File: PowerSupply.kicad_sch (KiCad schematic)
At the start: 3 parts

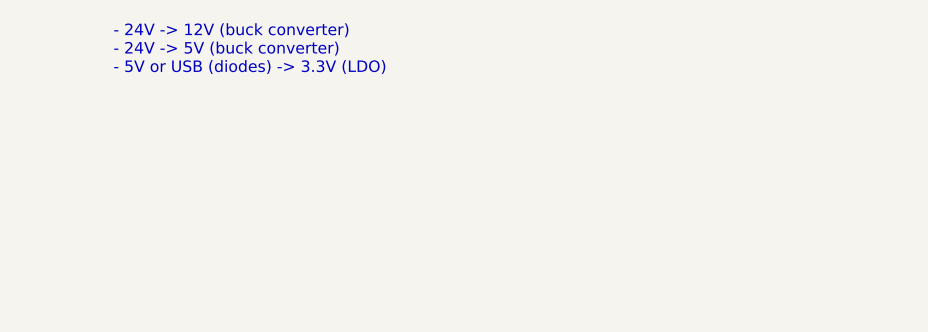
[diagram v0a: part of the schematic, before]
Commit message: Assigning a lot of values to components Change MOSFETS for different (correct) ones Copy Motor1 to Motor2-4 Guess max current per voltage on PowerSupply schema
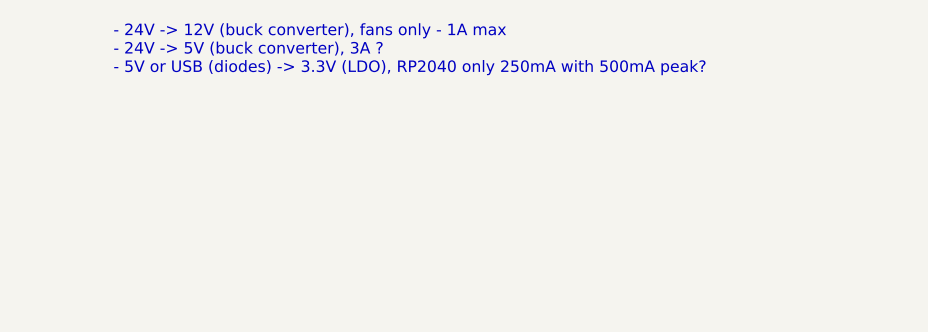
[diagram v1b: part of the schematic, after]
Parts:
- J?: footprint (none) -> Connector_USB:USB_C_Receptacle_GCT_USB4105-xx-A_16P_TopMnt_Horizontal; LCSC (none) -> C2765186
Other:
- note added: "- 24V -> 12V (buck converter), fans only - 1A max - 24V -> 5V (buck converter), 3A ? - 5V or USB (diodes) -> 3.3V (LDO), RP2040 only 250mA with 500mA peak?"
- note removed: "- 24V -> 12V (buck converter) - 24V -> 5V (buck converter) - 5V or USB (diodes) -> 3.3V (LDO)"
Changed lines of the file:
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@@
     (stroke (width 0) (type default))
   )
-  (text "- 24V -> 12V (buck converter)\n- 24V -> 5V (buck converter)\n- 5V or USB (diodes) -> 3.3V (LDO)"
+  (text "- 24V -> 12V (buck converter), fans only - 1A max\n- 24V -> 5V (buck converter), 3A ?\n- 5V or USB (diodes) -> 3.3V (LDO), RP2040 only 250mA with 500mA peak?"
     (at 30.48 34.29 0)
     (effects (font (size 1.27 1.27)) (justify left bottom))
@@
       )
       (project "Can3DPrinter4Motor"
-        (path "/cb4e159a-5c17-494a-ba7f-10e700f814f1/48301791-0cbb-476d-b990-e4256493ff46"
-          (reference "#PWR?") (unit 1)
-        )
         (path "/cb4e159a-5c17-494a-ba7f-10e700f814f1/03ab3e80-f454-40c8-8f97-43a0b791de0b"
           (reference "#PWR0402") (unit 1)
+        )
+        (path "/cb4e159a-5c17-494a-ba7f-10e700f814f1/48301791-0cbb-476d-b990-e4256493ff46"
+          (reference "#PWR0302") (unit 1)
         )
       )
@@
       (effects (font (size 1.27 1.27)))
     )
-    (property "Footprint" "" (at 38.1 165.1 0)
-      (effects (font (size 1.27 1.27)) hide)
-    )
-    (property "Datasheet" "https://www.usb.org/sites/default/files/documents/usb_type-c.zip" (at 38.1 165.1 0)
-      (effects (font (size 1.27 1.27)) hide)
-    )
-    (property "LCSC" "" (at 34.29 165.1 0)
+    (property "Footprint" "Connector_USB:USB_C_Receptacle_GCT_USB4105-xx-A_16P_TopMnt_Horizontal" (at 38.1 165.1 0)
+      (effects (font (size 1.27 1.27)) hide)
+    )
+    (property "Datasheet" "https://datasheet.lcsc.com/lcsc/2111231930_SHOU-HAN-TYPE-C-16PIN-2MD-073_C2765186.pdf" (at 38.1 165.1 0)
+      (effects (font (size 1.27 1.27)) hide)
+    )
+    (property "LCSC" "C2765186" (at 34.29 165.1 0)
       (effects (font (size 1.27 1.27)) hide)
     )
@@
     (instances
       (project "Can3DPrinter4Motor"
-        (path "/cb4e159a-5c17-494a-ba7f-10e700f814f1/48301791-0cbb-476d-b990-e4256493ff46"
+        (path "/cb4e159a-5c17-494a-ba7f-10e700f814f1/03ab3e80-f454-40c8-8f97-43a0b791de0b"
           (reference "J?") (unit 1)
         )
-        (path "/cb4e159a-5c17-494a-ba7f-10e700f814f1/03ab3e80-f454-40c8-8f97-43a0b791de0b"
-          (reference "J?") (unit 1)
+        (path "/cb4e159a-5c17-494a-ba7f-10e700f814f1/48301791-0cbb-476d-b990-e4256493ff46"
+          (reference "J301") (unit 1)
         )
       )
@@
           (reference "R?") (unit 1)
         )
-        (path "/cb4e159a-5c17-494a-ba7f-10e700f814f1/48301791-0cbb-476d-b990-e4256493ff46"
-          (reference "R?") (unit 1)
-        )
-        (path "/cb4e159a-5c17-494a-ba7f-10e700f814f1/03ab3e80-f454-40c8-8f97-43a0b791de0b"
-          (reference "R?") (unit 1)
+        (path "/cb4e159a-5c17-494a-ba7f-10e700f814f1/03ab3e80-f454-40c8-8f97-43a0b791de0b"
+          (reference "R?") (unit 1)
+        )
+        (path "/cb4e159a-5c17-494a-ba7f-10e700f814f1/48301791-0cbb-476d-b990-e4256493ff46"
+          (reference "R302") (unit 1)
         )
       )
@@
           (reference "R?") (unit 1)
         )
-        (path "/cb4e159a-5c17-494a-ba7f-10e700f814f1/48301791-0cbb-476d-b990-e4256493ff46"
-          (reference "R?") (unit 1)
-        )
-        (path "/cb4e159a-5c17-494a-ba7f-10e700f814f1/03ab3e80-f454-40c8-8f97-43a0b791de0b"
-          (reference "R?") (unit 1)
+        (path "/cb4e159a-5c17-494a-ba7f-10e700f814f1/03ab3e80-f454-40c8-8f97-43a0b791de0b"
+          (reference "R?") (unit 1)
+        )
+        (path "/cb4e159a-5c17-494a-ba7f-10e700f814f1/48301791-0cbb-476d-b990-e4256493ff46"
+          (reference "R301") (unit 1)
         )
       )
@@
       )
       (project "Can3DPrinter4Motor"
-        (path "/cb4e159a-5c17-494a-ba7f-10e700f814f1/48301791-0cbb-476d-b990-e4256493ff46"
-          (reference "#PWR?") (unit 1)
-        )
         (path "/cb4e159a-5c17-494a-ba7f-10e700f814f1/03ab3e80-f454-40c8-8f97-43a0b791de0b"
           (reference "#PWR0401") (unit 1)
         )
-      )
+        (path "/cb4e159a-5c17-494a-ba7f-10e700f814f1/48301791-0cbb-476d-b990-e4256493ff46"
+          (reference "#PWR0301") (unit 1)
+        )
+      )

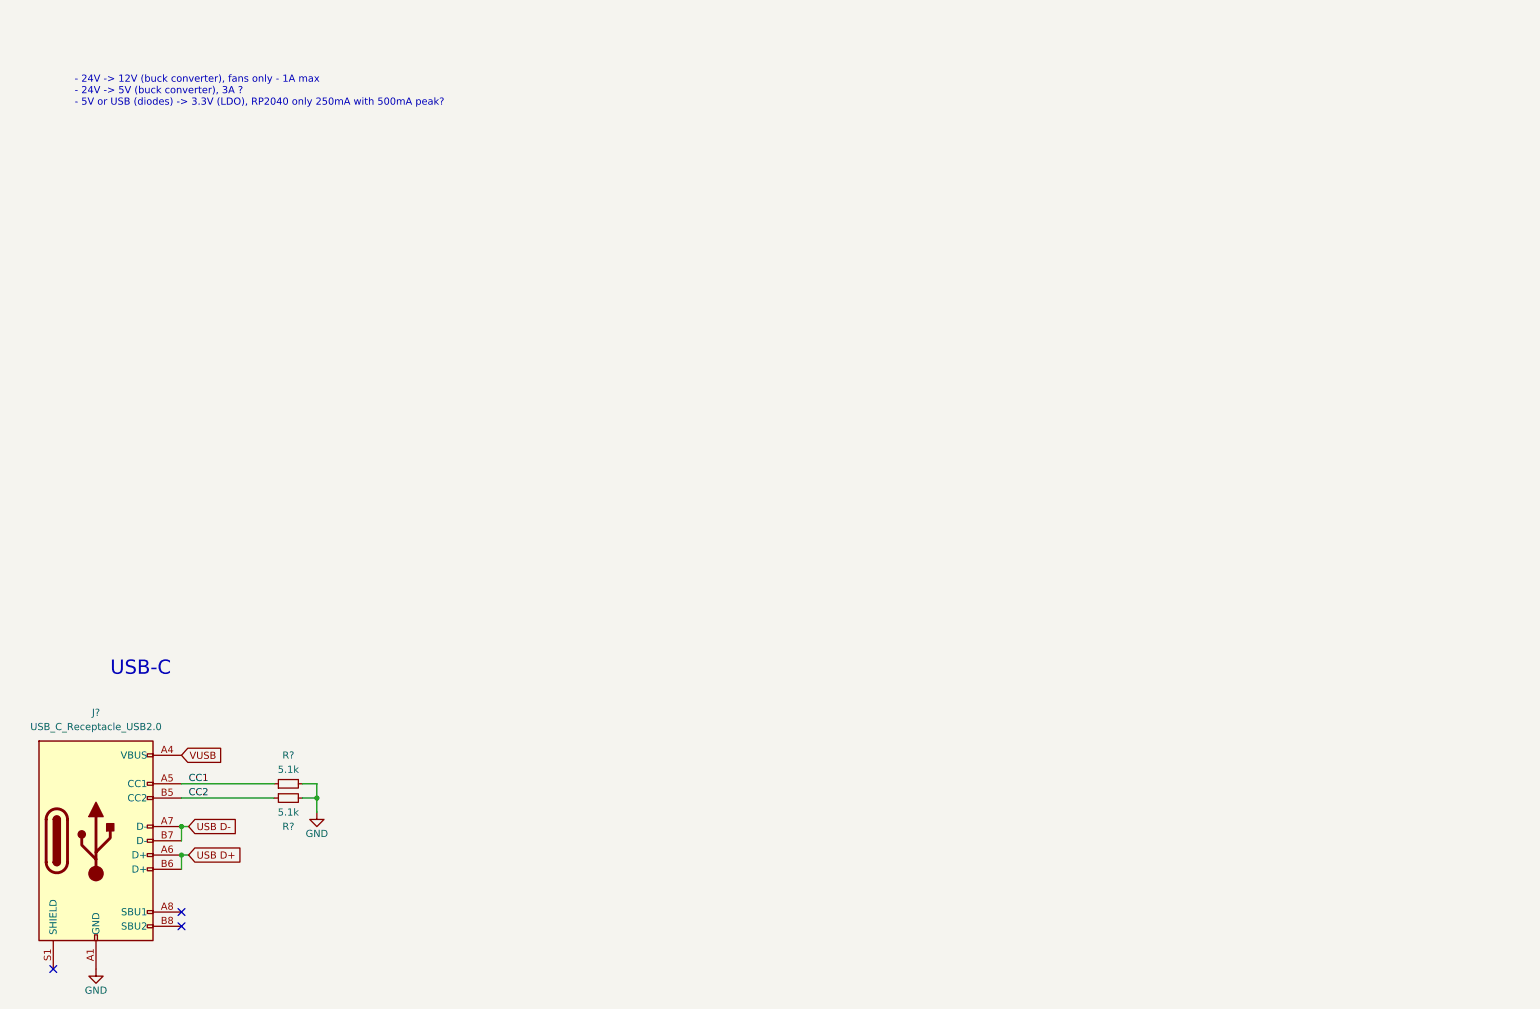
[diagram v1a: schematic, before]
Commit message: Complete schematics Assign every value (very few exceptions) Change TCM5160 from on-board to separate module Add fuses Add power supplies (LDO + 2x buck converter)
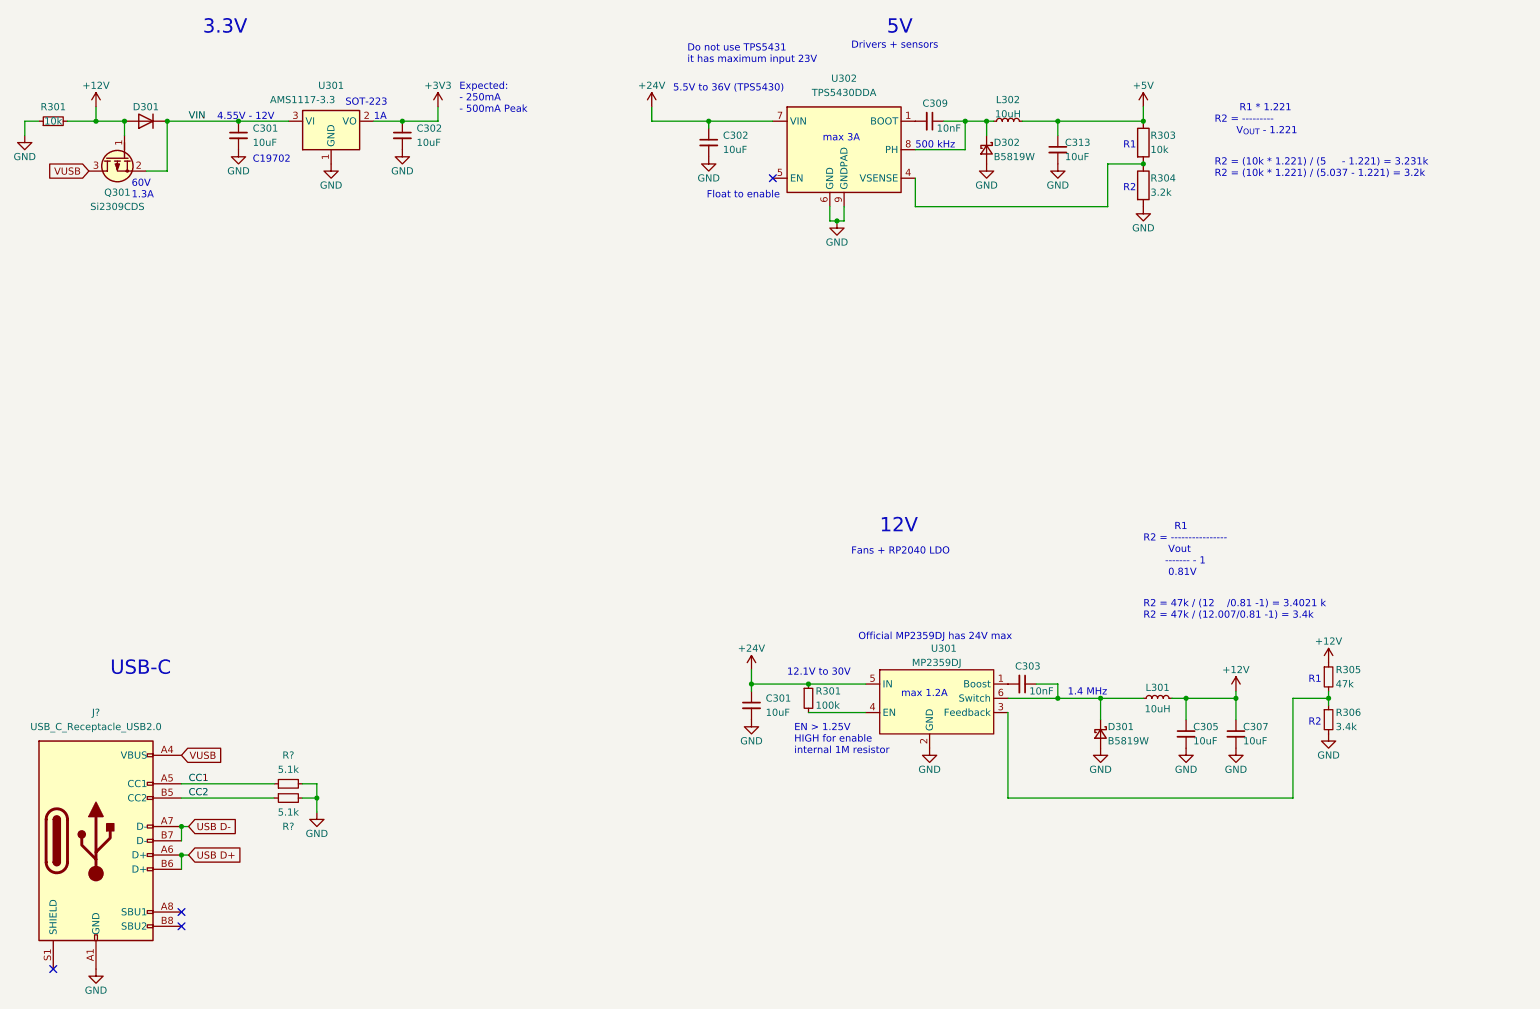
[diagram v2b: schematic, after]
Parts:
- added C301 (x2), C302 (x2), C305, C307, C313: 10uF, Capacitor_SMD:C_1206_3216Metric, symbol Device:C_Small
- added C303, C309: 10nF, Capacitor_SMD:C_0603_1608Metric, symbol Device:C_Small
- added D301, D302: B5819W, Diode_SMD:D_SOD-123, symbol Device:D_Schottky_Small
- added D301: D_Schottky, Diode_SMD:D_SMA, symbol Device:D
- added L301, L302: 10uH, Inductor_SMD:L_Sunlord_MWSA0503S, symbol Device:L_Small
- added Q301: Si2309CDS, Package_TO_SOT_SMD:SOT-23, symbol PCM_Transistor_MOSFET_AKL:Si2309CDS
- added R301: 100k, Resistor_SMD:R_0603_1608Metric, symbol Device:R_Small
- added R301: 10k, Resistor_SMD:R_0603_1608Metric, symbol Device:R_Small
- added R303: 10k, Resistor_SMD:R_0603_1608Metric, symbol Device:R
- added R304: 3.2k, Resistor_SMD:R_0603_1608Metric, symbol Device:R
- added R305: 47k, Resistor_SMD:R_0603_1608Metric, symbol Device:R_Small
- added R306: 3.4k, Resistor_SMD:R_0603_1608Metric, symbol Device:R_Small
- added U301: MP2359DJ, Package_TO_SOT_SMD:SOT-23-6, symbol Yautja:MP2359DJ
- added U301: AMS1117-3.3, Package_TO_SOT_SMD:SOT-223-3_TabPin2, symbol Regulator_Linear:NCP1117-3.3_SOT223
- added U302: TPS5430DDA, Package_SO:TI_SO-PowerPAD-8_ThermalVias, symbol Regulator_Switching:TPS5430DDA
- R? (x2): footprint (none) -> Resistor_SMD:R_0603_1608Metric; LCSC (none) -> C23186
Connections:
- net GND: now also C301.2, C301.2, C302.2, C302.2, C305.2, C307.2, C313.2, D301.2 (A), D302.2 (A), R301.1, R304.2, R306.2, U301.1 (GND), U301.2 (GND), U302.6 (GND), U302.9 (GNDPAD)
- net VUSB: now also Q301.3 (D)
- new net: R301.2, U301.4 (EN)
- new net: C303.2, U301.1 (Boost)
- new net: R305.2, R306.1, U301.3 (Feedback)
- new net: C303.1, D301.1 (K), L301.1, U301.6 (Switch)
- new net: R303.2, R304.1, U302.4 (VSENSE)
- new net: C309.1, D302.1 (K), L302.1, U302.8 (PH)
- new net: C309.2, U302.1 (BOOT)
- new net +12V: C305.1, C307.1, D301.2 (A), L301.2, Q301.1 (G), R301.2, R305.1
- new net +24V: C301.1, C302.1, R301.1, U301.5 (IN), U302.7 (VIN)
- new net +3V3: C302.1, U301.2 (VO)
- new net +5V: C313.1, L302.2, R303.1
- new net VIN: C301.1, D301.1 (K), Q301.2 (S), U301.3 (VI)
- no-connect marks 3 -> 4
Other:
- note added: "1.4 MHz"
- note added: "12.1V to 30V"
- note added: "12V"
- note added: "1A"
- note added: "3.3V"
- note added: "4.55V - 12V"
- note added: "5.5V to 36V (TPS5430)"
- note added: "500 kHz"
- note added: "5V"
- note added: "60V 1.3A"
- note added: "C19702"
- note added: "Do not use TPS5431 it has maximum input 23V"
- note added: "Drivers + sensors"
- note added: "EN > 1.25V HIGH for enable internal 1M resistor"
- note added: "Expected: - 250mA - 500mA Peak"
- note added: "Fans + RP2040 LDO"
- note added: "Float to enable"
- note added: "Official MP2359DJ has 24V max"
- note added: "R1"
- note added: "R1 * 1.221 R2 = --------- V_{OUT} - 1.221"
- note added: "R1 R2 = ---------------- Vout ------- - 1 0.81V"
- note added: "R2"
- note added: "R2 = (10k * 1.221) / (5 - 1.221) = 3.231k R2 = (10k * 1.221) / (5.037 - 1.221) = 3.2k"
- note added: "R2 = 47k / (12 /0.81 -1) = 3.4021 k R2 = 47k / (12.007/0.81 -1) = 3.4k"
- note added: "SOT-223"
- note added: "max 1.2A"
- note added: "max 3A"
- note removed: "- 24V -> 12V (buck converter), fans only - 1A max - 24V -> 5V (buck converter), 3A ? - 5V or USB (diodes) -> 3.3V (LDO), RP2040 only 250mA with 500mA peak?"
